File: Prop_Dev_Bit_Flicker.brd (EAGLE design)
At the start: 63.2 x 24.9 mm, 71 parts, among them J1 MF-CON-MICROUSB-RIGHT, J4 M20-7822046, J5 M20-7822046, U1 P8X32A-Q44, U2 FT230XQ-R, U3 TPS2113ADRBR, U4 CAT24C512WI-GT3, U5 MAX11613EUA+, U6 NCP1117LPST33T3G, U7 IRLML6401TRPBF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

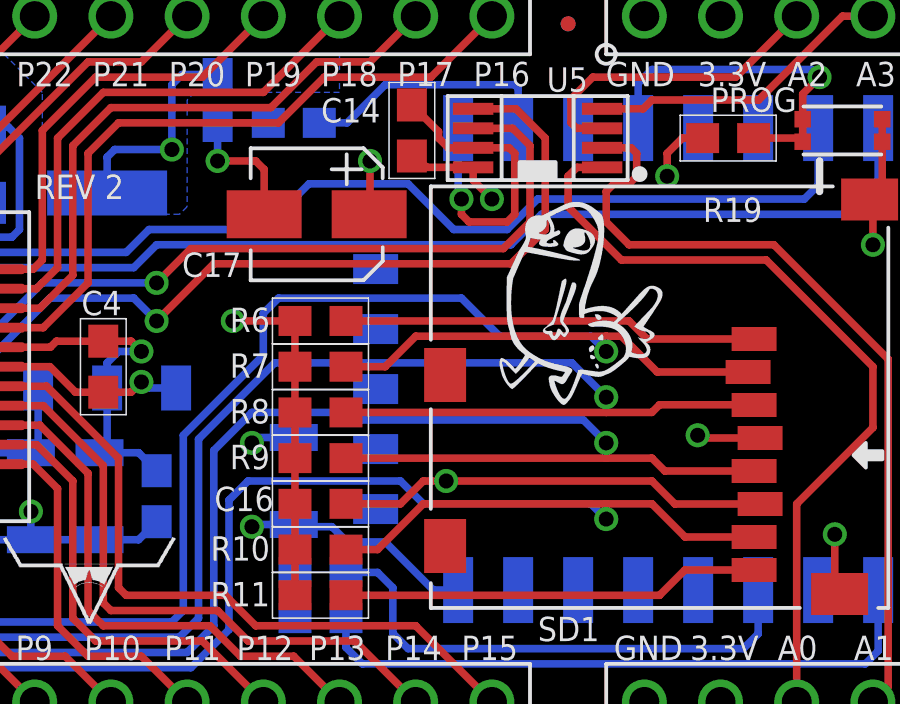
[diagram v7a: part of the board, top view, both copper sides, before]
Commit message: Fixed EP-12E and new camfiles.
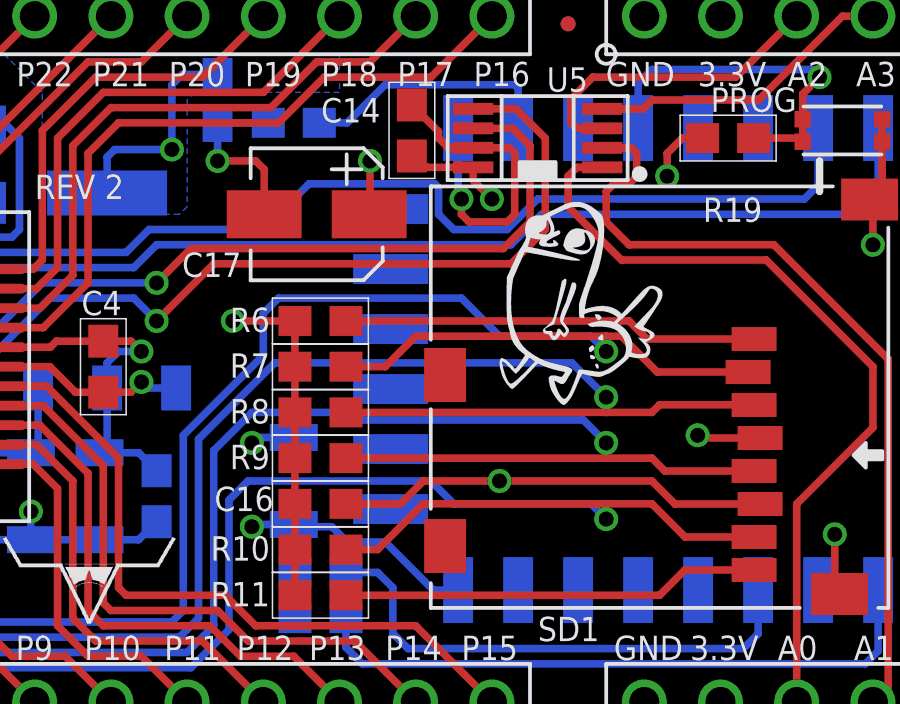
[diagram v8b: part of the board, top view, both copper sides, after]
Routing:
- net GND: track 141.1 -> 141.8 mm
- net WIFI_RX: track 55.6 -> 56.2 mm
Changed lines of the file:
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@@
 <wire x1="44.411" y1="7.62" x2="46.228" y2="7.62" width="0.254" layer="1"/>
 <wire x1="46.228" y1="7.62" x2="46.99" y2="8.382" width="0.254" layer="1"/>
-<wire x1="46.99" y1="8.382" x2="47.752" y2="8.382" width="0.254" layer="1"/>
-<via x="47.752" y="8.382" extent="1-16" drill="0.5"/>
-<wire x1="47.752" y1="8.382" x2="48.26" y2="8.382" width="0.254" layer="2"/>
+<wire x1="46.99" y1="8.382" x2="49.53" y2="8.382" width="0.254" layer="1"/>
+<via x="49.53" y="8.382" extent="1-16" drill="0.5"/>
+<wire x1="49.53" y1="8.382" x2="48.26" y2="8.382" width="0.254" layer="2"/>
 <wire x1="58.21525" y1="7.61475" x2="55.37725" y2="7.61475" width="0.254" layer="1"/>
 <wire x1="55.37725" y1="7.61475" x2="54.61" y2="8.382" width="0.254" layer="1"/>
-<wire x1="54.61" y1="8.382" x2="47.752" y2="8.382" width="0.254" layer="1"/>
+<wire x1="54.61" y1="8.382" x2="49.53" y2="8.382" width="0.254" layer="1"/>
 <wire x1="61.86525" y1="17.76475" x2="61.976" y2="17.654" width="0.254" layer="1"/>
 <wire x1="61.976" y1="17.654" x2="61.976" y2="16.256" width="0.254" layer="1"/>
@@
 <wire x1="40.513" y1="3.429" x2="40.513" y2="7.747" width="0.254" layer="16"/>
 <wire x1="40.513" y1="7.747" x2="41.148" y2="8.382" width="0.254" layer="16"/>
-<wire x1="41.148" y1="8.382" x2="46.228" y2="8.382" width="0.254" layer="16"/>
-<wire x1="46.228" y1="8.382" x2="46.99" y2="7.62" width="0.254" layer="16"/>
-<wire x1="46.99" y1="7.62" x2="52.578" y2="7.62" width="0.254" layer="16"/>
+<wire x1="41.148" y1="8.382" x2="47.244" y2="8.382" width="0.254" layer="16"/>
+<wire x1="47.244" y1="8.382" x2="48.006" y2="7.62" width="0.254" layer="16"/>
+<wire x1="48.006" y1="7.62" x2="52.578" y2="7.62" width="0.254" layer="16"/>
 <wire x1="52.578" y1="7.62" x2="53.086" y2="7.112" width="0.254" layer="16"/>
 <via x="53.086" y="7.112" extent="1-16" drill="0.5"/>
@@
 <wire x1="25.452" y1="16.692" x2="25.452" y2="22.3" width="0.254" layer="1"/>
 <wire x1="49.784" y1="16.764" x2="48.006" y2="16.764" width="0.254" layer="16"/>
-<wire x1="48.006" y1="16.764" x2="46.482" y2="18.288" width="0.254" layer="16"/>
-<wire x1="46.482" y1="18.288" x2="43.18" y2="18.288" width="0.254" layer="16"/>
+<wire x1="47.371" y1="18.288" x2="43.18" y2="18.288" width="0.254" layer="16"/>
 <wire x1="43.18" y1="18.288" x2="41.656" y2="16.764" width="0.254" layer="16"/>
 <wire x1="41.656" y1="16.764" x2="37.846" y2="16.764" width="0.254" layer="16"/>
@@
 <wire x1="24.257" y1="20.447" x2="23.876" y2="20.828" width="0.254" layer="16"/>
 <wire x1="23.876" y1="20.828" x2="23.876" y2="23.876" width="0.254" layer="16"/>
+<wire x1="47.371" y1="18.288" x2="47.498" y2="18.161" width="0.254" layer="16"/>
+<wire x1="47.498" y1="18.161" x2="47.498" y2="17.272" width="0.254" layer="16"/>
+<wire x1="47.498" y1="17.272" x2="48.006" y2="16.764" width="0.254" layer="16"/>
 </signal>
 <signal name="GPIO15">
